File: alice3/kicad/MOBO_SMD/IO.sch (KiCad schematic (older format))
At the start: 13 parts, among them CON1 SD_Card, P2 CONN_01X01, SW2 SOFT RESET, U6 MiniM4-D40

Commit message: replace MiniM4 with STM324F415RG directly
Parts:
- removed U6: MiniM4-D40, Housings_DIP:DIP-40_W15.24mm, symbol MiniM4-D40
- added U?: STM32F415RG, symbol STM32F415RG
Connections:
- wire segments 74 -> 49
- no-connect marks 6 -> 4
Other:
- moved on the sheet: R4, SW2

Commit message: Continuing to integrate STM32F415RG parts
Power circuit
STM32F415RG power and ground and BOOT pins
MicroSD card component and footprint
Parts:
- removed CON1: SD_Card, Pin_Headers:Pin_Header_Straight_1x10, symbol SD_Card
- removed P2: CONN_01X01, Pin_Headers:Pin_Header_Straight_1x01, symbol CONN_01X01
- added C10, C11, C6, C7: 22pF, symbol C_Small
- added C12, C13, C14, C15, C16: 100nF, symbol C_Small
- added C8, C9: 2.2µF, symbol C_Small
- added CON1: MicroSD, symbol MicroSD
- added JP1: Jumper_NO_Small, symbol Jumper_NO_Small
- added R17: 10k, Resistors_ThroughHole:Resistor_Horizontal_RM10mm, symbol R
- added Y2: 16MHz, symbol Crystal
- added Y3: 32.768KHz, symbol Crystal
- gave numbers to parts that had none: 1
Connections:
- wire segments 49 -> 81
- no-connect marks 4 -> 14
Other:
- moved on the sheet: C3, R5, R6, R7, R8

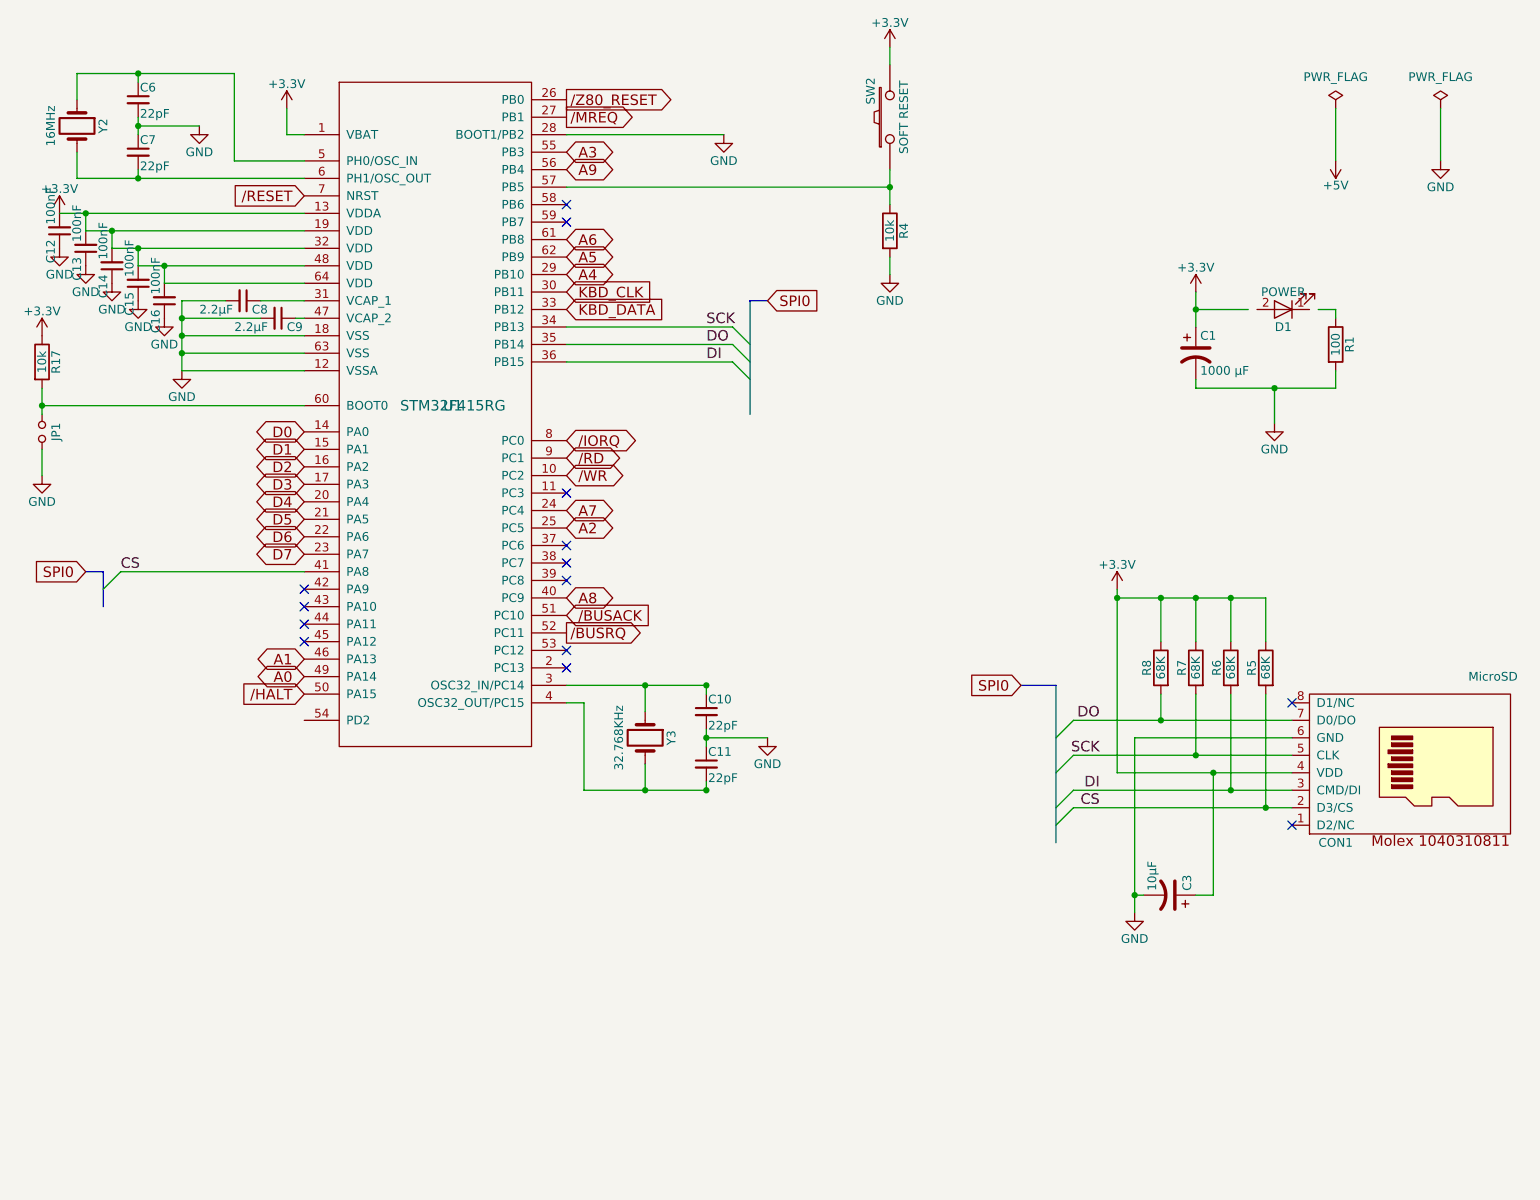
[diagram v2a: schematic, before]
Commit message: USB connector
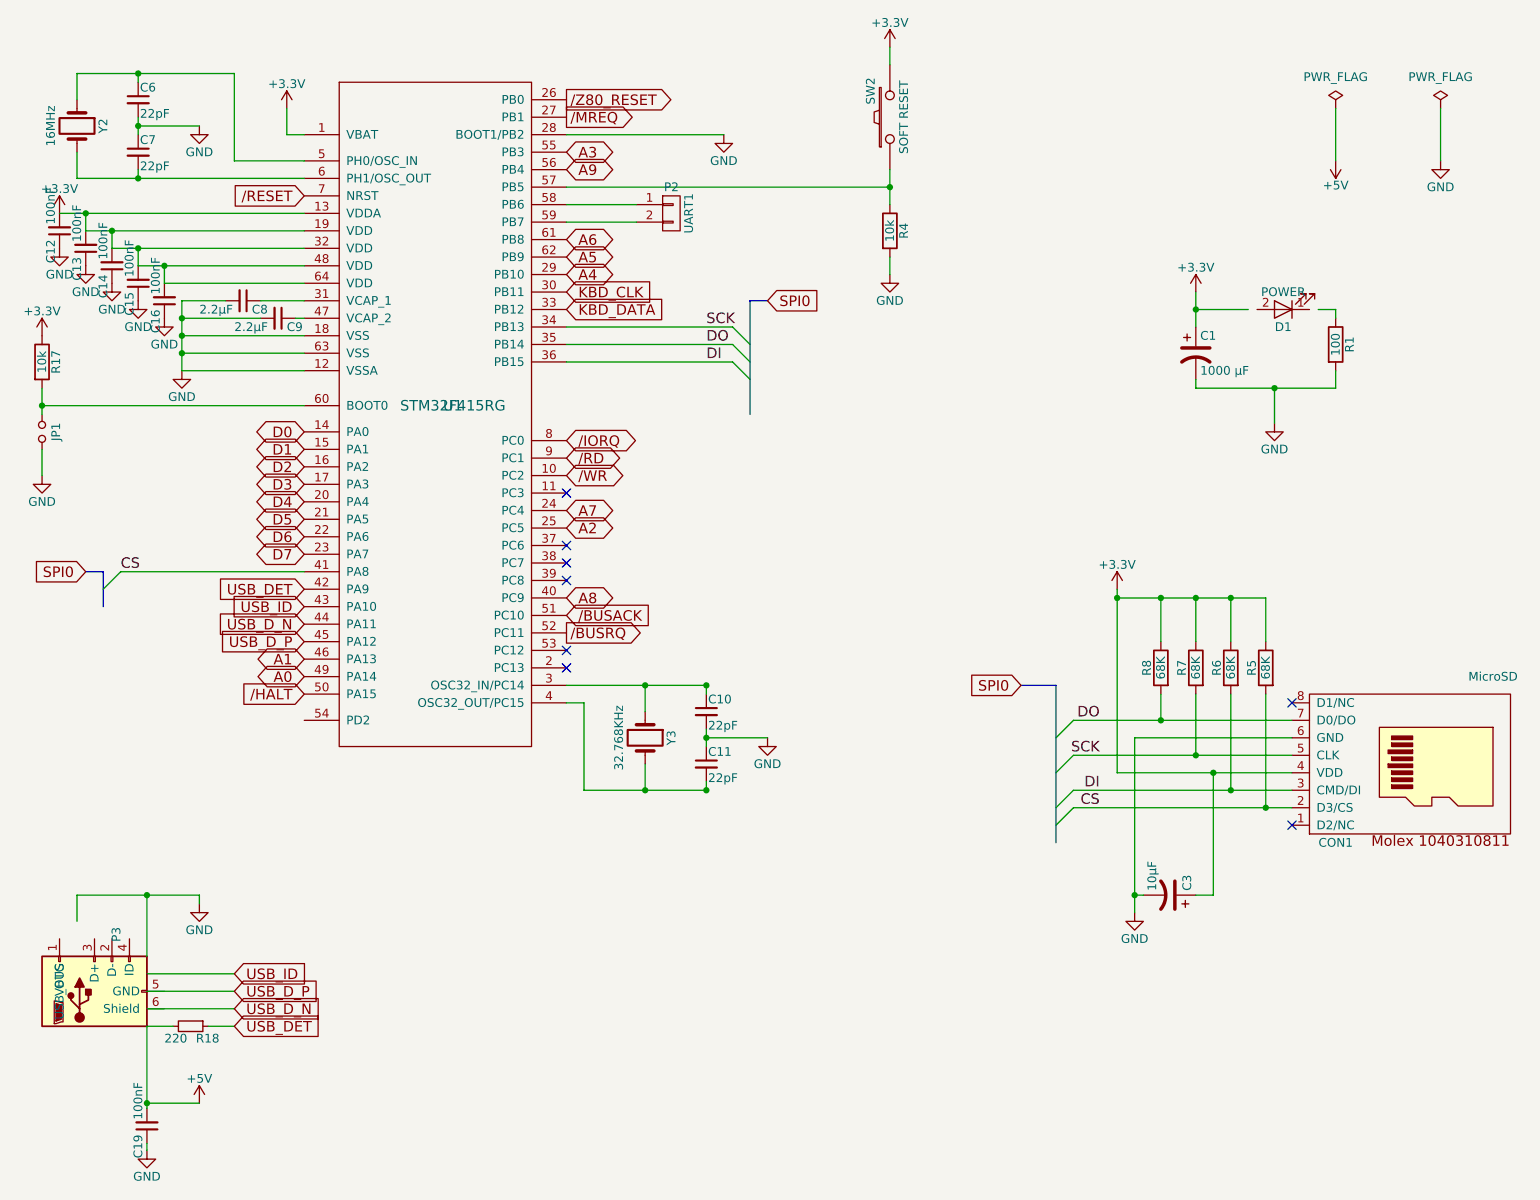
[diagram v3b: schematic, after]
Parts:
- added C19: 100nF, symbol C_Small
- added P2: UART1, symbol CONN_01X02
- added P3: USB_OTG, symbol USB_OTG
- added R18: 220, symbol R_Small
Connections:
- net labels added: USB_DET, USB_D_N, USB_D_P, USB_ID
- wire segments 81 -> 95
- no-connect marks 14 -> 8
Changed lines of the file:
@@
 $EndDescr
 $Comp
-L +3.3V #PWR016
+L +3.3V #PWR32
 U 1 1 5689970E
 P 5750 950
-F 0 "#PWR016" H 5750 800 50  0001 C CNN
+F 0 "#PWR32" H 5750 800 50  0001 C CNN
 F 1 "+3.3V" H 5750 1090 50  0000 C CNN
 F 2 "" H 5750 950 60  0000 C CNN
@@
 NoConn ~ 8050 4700
 $Comp
-L GND #PWR017
+L GND #PWR35
 U 1 1 56899C9B
 P 7150 5900
-F 0 "#PWR017" H 7150 5650 50  0001 C CNN
+F 0 "#PWR35" H 7150 5650 50  0001 C CNN
 F 1 "GND" H 7150 5750 50  0000 C CNN
 F 2 "" H 7150 5900 60  0000 C CNN
@@
 $EndComp
 $Comp
-L +3.3V #PWR018
+L +3.3V #PWR34
 U 1 1 56899CD4
 P 7050 4050
-F 0 "#PWR018" H 7050 3900 50  0001 C CNN
+F 0 "#PWR34" H 7050 3900 50  0001 C CNN
 F 1 "+3.3V" H 7050 4190 50  0000 C CNN
 F 2 "" H 7050 4050 60  0000 C CNN
@@
 $EndComp
 $Comp
-L GND #PWR019
+L GND #PWR33
 U 1 1 568A1142
 P 5750 2250
-F 0 "#PWR019" H 5750 2000 50  0001 C CNN
+F 0 "#PWR33" H 5750 2000 50  0001 C CNN
 F 1 "GND" H 5750 2100 50  0000 C CNN
 F 2 "" H 5750 2250 60  0000 C CNN
@@
 NoConn ~ 8050 5400
 $Comp
-L PWR_FLAG #FLG020
+L PWR_FLAG #FLG1
 U 1 1 56A07E43
 P 8300 1300
-F 0 "#FLG020" H 8300 1395 50  0001 C CNN
+F 0 "#FLG1" H 8300 1395 50  0001 C CNN
 F 1 "PWR_FLAG" H 8300 1480 50  0000 C CNN
 F 2 "" H 8300 1300 50  0000 C CNN
@@
 $EndComp
 $Comp
-L +5V #PWR021
+L +5V #PWR38
 U 1 1 56A07E73
 P 8300 1600
-F 0 "#PWR021" H 8300 1450 50  0001 C CNN
+F 0 "#PWR38" H 8300 1450 50  0001 C CNN
 F 1 "+5V" H 8300 1740 50  0000 C CNN
 F 2 "" H 8300 1600 50  0000 C CNN
@@
 $EndComp
 $Comp
-L PWR_FLAG #FLG022
+L PWR_FLAG #FLG2
 U 1 1 56A0800D
 P 8900 1300
-F 0 "#FLG022" H 8900 1395 50  0001 C CNN
+F 0 "#FLG2" H 8900 1395 50  0001 C CNN
 F 1 "PWR_FLAG" H 8900 1480 50  0000 C CNN
 F 2 "" H 8900 1300 50  0000 C CNN
@@
 $EndComp
 $Comp
-L GND #PWR023
+L GND #PWR39
 U 1 1 56A08038
 P 8900 1600
-F 0 "#PWR023" H 8900 1350 50  0001 C CNN
+F 0 "#PWR39" H 8900 1350 50  0001 C CNN
 F 1 "GND" H 8900 1450 50  0000 C CNN
 F 2 "" H 8900 1600 50  0000 C CNN
@@
 $EndComp
 $Comp
-L GND #PWR024
+L GND #PWR37
 U 1 1 56A0883B
 P 7950 3100
-F 0 "#PWR024" H 7950 2850 50  0001 C CNN
+F 0 "#PWR37" H 7950 2850 50  0001 C CNN
 F 1 "GND" H 7950 2950 50  0000 C CNN
 F 2 "" H 7950 3100 50  0000 C CNN
@@
 $EndComp
 $Comp
-L +3.3V #PWR025
+L +3.3V #PWR36
 U 1 1 56A08841
 P 7500 2350
-F 0 "#PWR025" H 7500 2200 50  0001 C CNN
+F 0 "#PWR36" H 7500 2200 50  0001 C CNN
 F 1 "+3.3V" H 7500 2490 50  0000 C CNN
 F 2 "" H 7500 2350 50  0000 C CNN
@@
 F 3 "" H 8300 2650 50  0000 C CNN
 	1    8300 2650
-	1    0    0    -1
-$EndComp
-$Comp
-L STM32F415RG U?
-U 1 1 56B635D1
-P 3250 3000
-AR Path="/56B635D1" Ref="U?"  Part="1"
-AR Path="/568DBAE1/56B635D1" Ref="U1"  Part="1"
-F 0 "U1" H 3250 3000 60  0000 C CNN
-F 1 "STM32F415RG" H 3250 3000 60  0000 C CNN
-F 2 "" H 3250 3000 60  0000 C CNN
-F 3 "" H 3250 3000 60  0000 C CNN
-	1    3250 3000
 	1    0    0    -1
 $EndComp
@@
 A0
 $Comp
-L GND #PWR026
+L GND #PWR25
 U 1 1 56B85293
 P 1700 2800
-F 0 "#PWR026" H 1700 2550 50  0001 C CNN
+F 0 "#PWR25" H 1700 2550 50  0001 C CNN
 F 1 "GND" H 1700 2650 50  0000 C CNN
 F 2 "" H 1700 2800 60  0000 C CNN
@@
 $EndComp
 $Comp
-L +3.3V #PWR027
+L +3.3V #PWR29
 U 1 1 56BA49D2
 P 2300 1300
-F 0 "#PWR027" H 2300 1150 50  0001 C CNN
+F 0 "#PWR29" H 2300 1150 50  0001 C CNN
 F 1 "+3.3V" H 2300 1440 50  0000 C CNN
 F 2 "" H 2300 1300 60  0000 C CNN
@@
 $EndComp
 $Comp
-L GND #PWR028
+L GND #PWR26
 U 1 1 56BA4C6B
 P 1800 1400
-F 0 "#PWR028" H 1800 1150 50  0001 C CNN
+F 0 "#PWR26" H 1800 1150 50  0001 C CNN
 F 1 "GND" H 1800 1250 50  0000 C CNN
 F 2 "" H 1800 1400 60  0000 C CNN
@@
 $EndComp
 $Comp
-L GND #PWR029
+L GND #PWR30
 U 1 1 56BA634D
 P 4800 1450
-F 0 "#PWR029" H 4800 1200 50  0001 C CNN
+F 0 "#PWR30" H 4800 1200 50  0001 C CNN
 F 1 "GND" H 4800 1300 50  0000 C CNN
 F 2 "" H 4800 1450 60  0000 C CNN
@@
 $EndComp
 $Comp
-L +3.3V #PWR030
+L +3.3V #PWR16
 U 1 1 56BA6501
 P 900 2600
-F 0 "#PWR030" H 900 2450 50  0001 C CNN
+F 0 "#PWR16" H 900 2450 50  0001 C CNN
 F 1 "+3.3V" H 900 2740 50  0000 C CNN
 F 2 "" H 900 2600 60  0000 C CNN
@@
 $EndComp
 $Comp
-L GND #PWR031
+L GND #PWR17
 U 1 1 56BA66E5
 P 900 3400
-F 0 "#PWR031" H 900 3150 50  0001 C CNN
+F 0 "#PWR17" H 900 3150 50  0001 C CNN
 F 1 "GND" H 900 3250 50  0000 C CNN
 F 2 "" H 900 3400 60  0000 C CNN
@@
 $EndComp
 $Comp
-L GND #PWR032
+L GND #PWR31
 U 1 1 56BA69C4
 P 5050 4900
-F 0 "#PWR032" H 5050 4650 50  0001 C CNN
+F 0 "#PWR31" H 5050 4650 50  0001 C CNN
 F 1 "GND" H 5050 4750 50  0000 C CNN
 F 2 "" H 5050 4900 60  0000 C CNN
@@
 $EndComp
 $Comp
-L +3.3V #PWR033
+L +3.3V #PWR18
 U 1 1 56BA9EA1
 P 1000 1900
-F 0 "#PWR033" H 1000 1750 50  0001 C CNN
+F 0 "#PWR18" H 1000 1750 50  0001 C CNN
 F 1 "+3.3V" H 1000 2040 50  0000 C CNN
 F 2 "" H 1000 1900 60  0000 C CNN
@@
 $EndComp
 $Comp
-L GND #PWR034
+L GND #PWR24
 U 1 1 56BAAE8C
 P 1600 2500
-F 0 "#PWR034" H 1600 2250 50  0001 C CNN
+F 0 "#PWR24" H 1600 2250 50  0001 C CNN
 F 1 "GND" H 1600 2350 50  0000 C CNN
 F 2 "" H 1600 2500 60  0000 C CNN
@@
 $EndComp
 $Comp
-L GND #PWR035
+L GND #PWR22
 U 1 1 56BAAEE8
 P 1450 2400
-F 0 "#PWR035" H 1450 2150 50  0001 C CNN
+F 0 "#PWR22" H 1450 2150 50  0001 C CNN
 F 1 "GND" H 1450 2250 50  0000 C CNN
 F 2 "" H 1450 2400 60  0000 C CNN
@@
 $EndComp
 $Comp
-L GND #PWR036
+L GND #PWR21
 U 1 1 56BAAF44
 P 1300 2300
-F 0 "#PWR036" H 1300 2050 50  0001 C CNN
+F 0 "#PWR21" H 1300 2050 50  0001 C CNN
 F 1 "GND" H 1300 2150 50  0000 C CNN
 F 2 "" H 1300 2300 60  0000 C CNN
@@
 $EndComp
 $Comp
-L GND #PWR037
+L GND #PWR20
 U 1 1 56BAAFA0
 P 1150 2200
-F 0 "#PWR037" H 1150 1950 50  0001 C CNN
+F 0 "#PWR20" H 1150 1950 50  0001 C CNN
 F 1 "GND" H 1150 2050 50  0000 C CNN
 F 2 "" H 1150 2200 60  0000 C CNN
@@
 $EndComp
 $Comp
-L GND #PWR038
+L GND #PWR19
 U 1 1 56BAAFFC
 P 1000 2100
-F 0 "#PWR038" H 1000 1850 50  0001 C CNN
+F 0 "#PWR19" H 1000 1850 50  0001 C CNN
 F 1 "GND" H 1000 1950 50  0000 C CNN
 F 2 "" H 1000 2100 60  0000 C CNN
@@
 	1150 2000 2400 2000
 Wire Wire Line
-	2400 2100 1300 2100
+	1300 2100 2400 2100
 Wire Wire Line
 	1450 2200 2400 2200
@@
 NoConn ~ 3900 4400
 NoConn ~ 3900 4500
-NoConn ~ 2400 4050
-NoConn ~ 2400 4150
-NoConn ~ 2400 4250
-NoConn ~ 2400 4350
-NoConn ~ 3900 1850
-NoConn ~ 3900 1950
+$Comp
+L CONN_01X02 P2
+U 1 1 56BAA324
+P 4500 1900
+F 0 "P2" H 4500 2050 50  0000 C CNN
+F 1 "UART1" V 4600 1900 50  0000 C CNN
+F 2 "" H 4500 1900 60  0000 C CNN
+F 3 "" H 4500 1900 60  0000 C CNN
+	1    4500 1900
+	1    0    0    -1
+$EndComp
+Wire Wire Line
+	3900 1850 4300 1850
+Wire Wire Line
+	3900 1950 4300 1950
+$Comp
+L USB_OTG P3
+U 1 1 56BAA76F
+P 1200 6350
+F 0 "P3" H 1525 6225 50  0000 C CNN
+F 1 "USB_OTG" H 1200 6550 50  0000 C CNN
+F 2 "" V 1150 6250 60  0000 C CNN
+F 3 "" V 1150 6250 60  0000 C CNN
+	1    1200 6350
+	0    -1   -1   0
+$EndComp
+$Comp
+L STM32F415RG U?
+U 1 1 56B635D1
+P 3250 3000
+AR Path="/56B635D1" Ref="U?"  Part="1"
+AR Path="/568DBAE1/56B635D1" Ref="U1"  Part="1"
+F 0 "U1" H 3250 3000 60  0000 C CNN
+F 1 "STM32F415RG" H 3250 3000 60  0000 C CNN
+F 2 "" H 3250 3000 60  0000 C CNN
+F 3 "" H 3250 3000 60  0000 C CNN
+	1    3250 3000
+	1    0    0    -1
+$EndComp
+Text GLabel 2400 4050 0    60   Input ~ 0
+USB_DET
+Text GLabel 2400 4150 0    60   Input ~ 0
+USB_ID
+Text GLabel 2400 4250 0    60   Input ~ 0
+USB_D_N
+Text GLabel 2400 4350 0    60   Input ~ 0
+USB_D_P
+Text GLabel 2000 6550 2    60   Input ~ 0
+USB_DET
+Text GLabel 2000 6250 2    60   Input ~ 0
+USB_ID
+Text GLabel 2000 6450 2    60   Input ~ 0
+USB_D_N
+Text GLabel 2000 6350 2    60   Input ~ 0
+USB_D_P
+$Comp
+L GND #PWR27
+U 1 1 56BAB684
+P 1800 5850
+F 0 "#PWR27" H 1800 5600 50  0001 C CNN
+F 1 "GND" H 1800 5700 50  0000 C CNN
+F 2 "" H 1800 5850 60  0000 C CNN
+F 3 "" H 1800 5850 60  0000 C CNN
+	1    1800 5850
+	1    0    0    -1
+$EndComp
+Wire Wire Line
+	1500 6150 1500 5800
+Wire Wire Line
+	1100 5800 1800 5800
+Wire Wire Line
+	1100 5950 1100 5800
+Connection ~ 1500 5800
+Wire Wire Line
+	1500 6250 2000 6250
+Wire Wire Line
+	1500 6350 2000 6350
+Wire Wire Line
+	1500 6450 2000 6450
+$Comp
+L +5V #PWR28
+U 1 1 56BABB53
+P 1800 6990
+F 0 "#PWR28" H 1800 6840 50  0001 C CNN
+F 1 "+5V" H 1800 7130 50  0000 C CNN
+F 2 "" H 1800 6990 60  0000 C CNN
+F 3 "" H 1800 6990 60  0000 C CNN
+	1    1800 6990
+	1    0    0    -1
+$EndComp
+Wire Wire Line
+	1500 6550 1500 7020
+Wire Wire Line
+	1500 6990 1800 6990
+Wire Wire Line
+	1800 5800 1800 5850
+$Comp
+L R_Small R18
+U 1 1 56BAC147
+P 1750 6550
+F 0 "R18" V 1820 6580 50  0000 L CNN
+F 1 "220" V 1820 6400 50  0000 L CNN
+F 2 "" H 1750 6550 60  0000 C CNN
+F 3 "" H 1750 6550 60  0000 C CNN
+	1    1750 6550
+	0    1    1    0
+$EndComp
+Wire Wire Line
+	1500 6550 1650 6550
+Wire Wire Line
+	1850 6550 2000 6550
+$Comp
+L GND #PWR23
+U 1 1 56BAC7E3
+P 1500 7260
+F 0 "#PWR23" H 1500 7010 50  0001 C CNN
+F 1 "GND" H 1500 7110 50  0000 C CNN
+F 2 "" H 1500 7260 60  0000 C CNN
+F 3 "" H 1500 7260 60  0000 C CNN
+	1    1500 7260
+	1    0    0    -1
+$EndComp
+$Comp
+L C_Small C19
+U 1 1 56BAC974
+P 1500 7120
+F 0 "C19" V 1550 7170 50  0000 L CNN
+F 1 "100nF" V 1550 6870 50  0000 L CNN
+F 2 "" H 1500 7120 60  0000 C CNN
+F 3 "" H 1500 7120 60  0000 C CNN
+	1    1500 7120
+	-1   0    0    1
+$EndComp
+Connection ~ 1500 6990
+Wire Wire Line
+	1500 7220 1500 7260
 $EndSCHEMATC

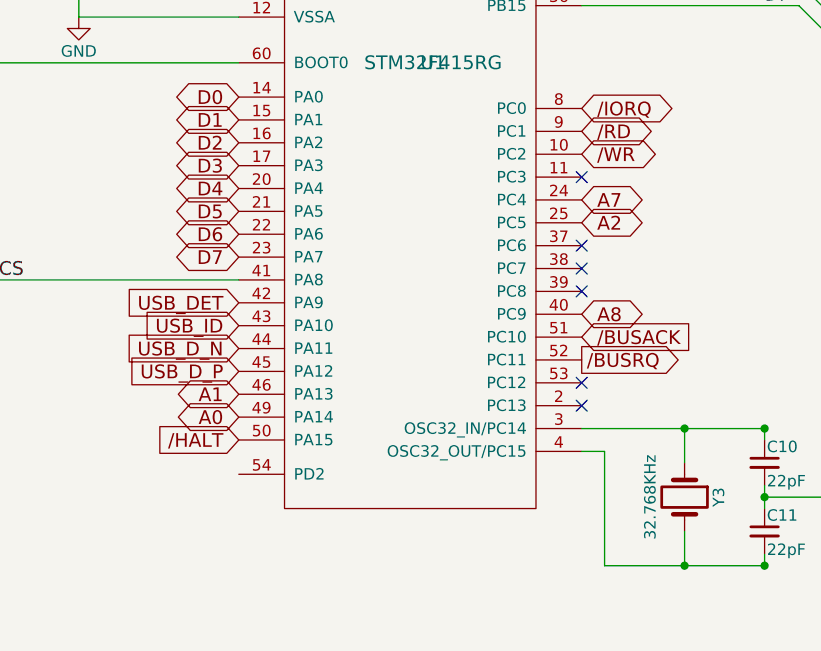
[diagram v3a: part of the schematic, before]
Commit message: Run all address lines to ARM UART header
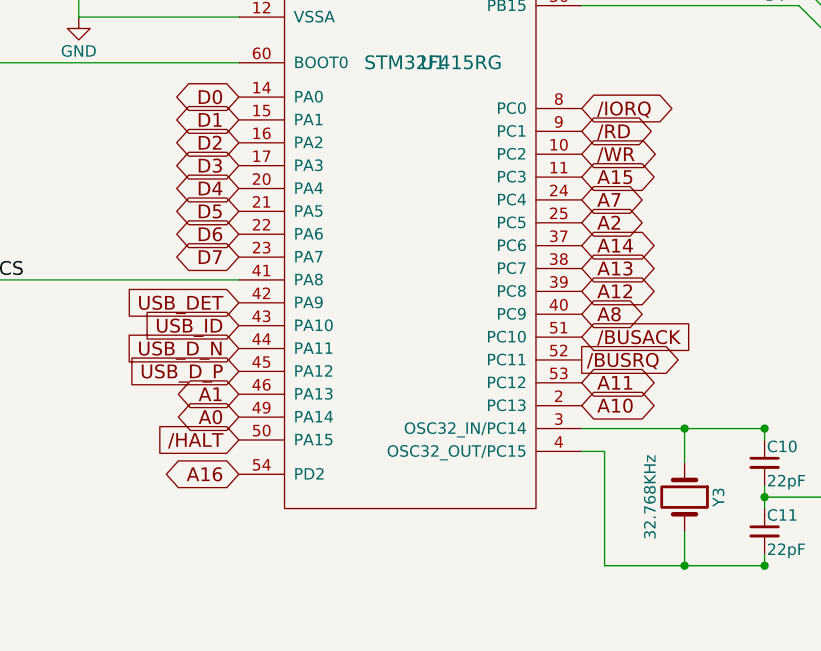
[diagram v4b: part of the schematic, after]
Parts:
- U1: footprint (none) -> Housings_QFP:LQFP-64_10x10mm_Pitch0.5mm
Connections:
- net labels added: A10, A11, A12, A13, A14, A15, A16
- no-connect marks 8 -> 2

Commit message: Add footprint for microUSB from SnapEDA
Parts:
- P3: footprint (none) -> snapeda_conn:10118192-0001LF
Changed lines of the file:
@@
 F 0 "P3" H 1525 6225 50  0000 C CNN
 F 1 "USB_OTG" H 1200 6550 50  0000 C CNN
-F 2 "" V 1150 6250 60  0001 C CNN
+F 2 "snapeda_conn:10118192-0001LF" V 1150 6250 60  0001 C CNN
 F 3 "" V 1150 6250 60  0000 C CNN
 	1    1200 6350
